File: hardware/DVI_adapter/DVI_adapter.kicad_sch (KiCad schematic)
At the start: 58 parts, among them J1 DF12NB(3.0)-30DS-0.5V(51), J2 DF12NB(3.0)-30DS-0.5V(51), J3 FPC Cable connector 1x20, U1 TXS0102DQE, U2 HE9009M6R, U2 TFP410

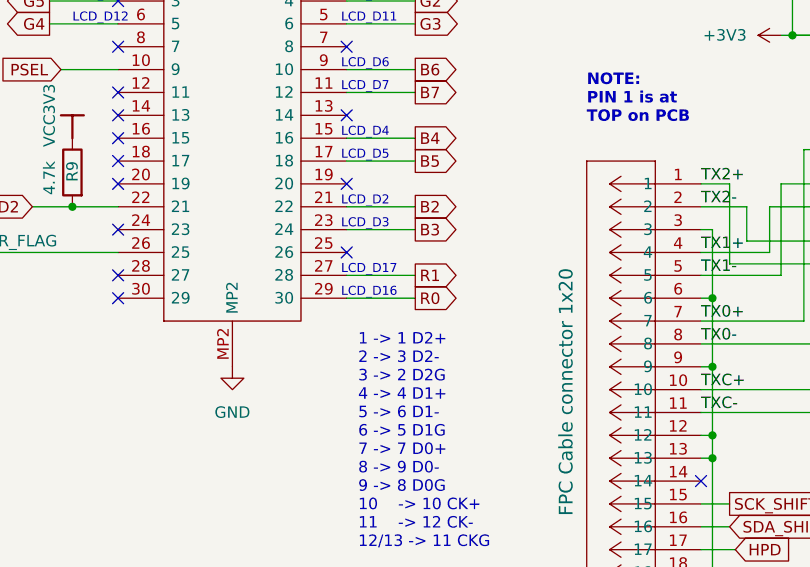
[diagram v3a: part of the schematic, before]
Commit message: fix R0/R1 mixup
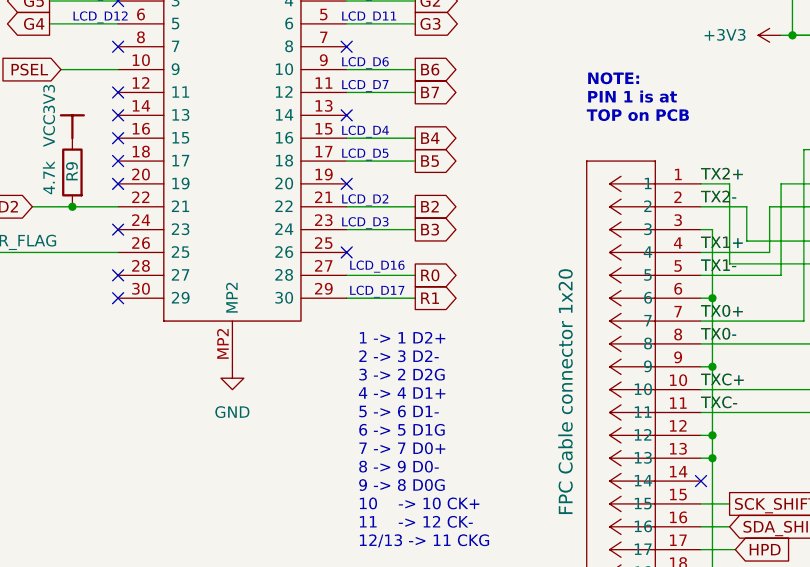
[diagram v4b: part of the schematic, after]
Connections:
- net R0: now also J2.27 (28); no longer J2.29 (30)
- net R1: now also J2.29 (30); no longer J2.27 (28)
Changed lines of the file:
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@@
+		)
+	)
+	(text "South connector"
+		(exclude_from_sim no)
+		(at 43.942 106.68 0)
+		(effects
+			(font
+				(size 1.27 1.27)
+			)
+			(justify right bottom)
+		)
+	)
+	(text "LCD_D15"
+		(exclude_from_sim no)
+		(at 61.595 78.74 0)
+		(effects
+			(font
+				(size 1 1)
+			)
+			(justify left bottom)
+		)
+	)
+	(text "LCD_D5"
+		(exclude_from_sim no)
+		(at 60.325 134.62 0)
+		(effects
+			(font
+				(size 1 1)
+			)
+			(justify left bottom)
+		)
+	)
+	(text "1 -> 1 D2+\n2 -> 3 D2-\n3 -> 2 D2G\n4 -> 4 D1+\n5 -> 6 D1-\n6 -> 5 D1G\n7 -> 7 D0+\n8 -> 9 D0-\n9 -> 8 D0G\n10    -> 10 CK+\n11    -> 12 CK-\n12/13 -> 11 CKG\n\n14 -> 13 CEC\n      14 NC\n15 -> 15 SCL\n16 -> 16 SDA\n      17 GND\n17 -> 19 HPD\n18/19/20 -> 18 +5V\nGND   20 SHIELD"
+		(exclude_from_sim no)
+		(at 62.23 175.006 0)
+		(effects
+			(font
+				(size 1.27 1.27)
+			)
+			(justify left)
+		)
+	)
+	(text "North connector"
+		(exclude_from_sim no)
+		(at 44.196 44.196 0)
+		(effects
+			(font
+				(size 1.27 1.27)
+			)
+			(justify right bottom)
+		)
+	)
+	(text "LCD_D1"
+		(exclude_from_sim no)
+		(at 31.75 50.8 0)
+		(effects
+			(font
+				(size 1 1)
+			)
+			(justify left bottom)
+		)
+	)
+	(text "LCD_D13"
+		(exclude_from_sim no)
+		(at 30.48 116.84 0)
+		(effects
+			(font
+				(size 1 1)
+			)
+			(justify left bottom)
+		)
+	)
+	(text "LCD_D9"
+		(exclude_from_sim no)
+		(at 31.75 66.04 0)
+		(effects
+			(font
+				(size 1 1)
+			)
+			(justify left bottom)
+		)
+	)
+	(text "LCD_D2"
+		(exclude_from_sim no)
+		(at 60.325 139.7 0)
+		(effects
+			(font
+				(size 1 1)
+			)
+			(justify left bottom)
+		)
+	)
+	(text "LCD_D18"
+		(exclude_from_sim no)
+		(at 61.595 68.58 0)
+		(effects
+			(font
+				(size 1 1)
+			)
+			(justify left bottom)
 		)
 	)
 	(text "LCD_D16"
 		(exclude_from_sim no)
-		(at 60.325 149.86 0)
-		(effects
-			(font
-				(size 1 1)
-			)
-			(justify left bottom)
-		)
-	)
-	(text "LCD_D17"
-		(exclude_from_sim no)
-		(at 60.325 147.32 0)
-		(effects
-			(font
-				(size 1 1)
-			)
-			(justify left bottom)
-		)
-	)
-	(text "South connector"
-		(exclude_from_sim no)
-		(at 43.942 106.68 0)
-		(effects
-			(font
-				(size 1.27 1.27)
-			)
-			(justify right bottom)
-		)
-	)
-	(text "LCD_D15"
-		(exclude_from_sim no)
-		(at 61.595 78.74 0)
-		(effects
-			(font
-				(size 1 1)
-			)
-			(justify left bottom)
-		)
-	)
-	(text "LCD_D5"
-		(exclude_from_sim no)
-		(at 60.325 134.62 0)
-		(effects
-			(font
-				(size 1 1)
-			)
-			(justify left bottom)
-		)
-	)
-	(text "1 -> 1 D2+\n2 -> 3 D2-\n3 -> 2 D2G\n4 -> 4 D1+\n5 -> 6 D1-\n6 -> 5 D1G\n7 -> 7 D0+\n8 -> 9 D0-\n9 -> 8 D0G\n10    -> 10 CK+\n11    -> 12 CK-\n12/13 -> 11 CKG\n\n14 -> 13 CEC\n      14 NC\n15 -> 15 SCL\n16 -> 16 SDA\n      17 GND\n17 -> 19 HPD\n18/19/20 -> 18 +5V\nGND   20 SHIELD"
-		(exclude_from_sim no)
-		(at 62.23 175.006 0)
-		(effects
-			(font
-				(size 1.27 1.27)
-			)
-			(justify left)
-		)
-	)
-	(text "North connector"
-		(exclude_from_sim no)
-		(at 44.196 44.196 0)
-		(effects
-			(font
-				(size 1.27 1.27)
-			)
-			(justify right bottom)
-		)
-	)
-	(text "LCD_D1"
-		(exclude_from_sim no)
-		(at 31.75 50.8 0)
-		(effects
-			(font
-				(size 1 1)
-			)
-			(justify left bottom)
-		)
-	)
-	(text "LCD_D13"
-		(exclude_from_sim no)
-		(at 30.48 116.84 0)
-		(effects
-			(font
-				(size 1 1)
-			)
-			(justify left bottom)
-		)
-	)
-	(text "LCD_D9"
-		(exclude_from_sim no)
-		(at 31.75 66.04 0)
-		(effects
-			(font
-				(size 1 1)
-			)
-			(justify left bottom)
-		)
-	)
-	(text "LCD_D2"
-		(exclude_from_sim no)
-		(at 60.325 139.7 0)
-		(effects
-			(font
-				(size 1 1)
-			)
-			(justify left bottom)
-		)
-	)
-	(text "LCD_D18"
-		(exclude_from_sim no)
-		(at 61.595 68.58 0)
+		(at 61.214 147.066 0)
 		(effects
 			(font
@@
 		)
 	)
+	(text "LCD_D17"
+		(exclude_from_sim no)
+		(at 61.214 149.86 0)
+		(effects
+			(font
+				(size 1 1)
+			)
+			(justify left bottom)
+		)
+	)
 	(text "NOTE:\nPIN 1 is at \nTOP on PCB"
 		(exclude_from_sim no)
@@
 		)
 	)
+	(global_label "R0"
+		(shape output)
+		(at 68.58 147.32 0)
+		(fields_autoplaced yes)
+		(effects
+			(font
+				(size 1.27 1.27)
+			)
+			(justify left)
+		)
+		(property "Intersheetrefs" "${INTERSHEET_REFS}"
+			(at 74.0447 147.32 0)
+			(effects
+				(font
+					(size 1.27 1.27)
+				)
+				(justify left)
+				(hide yes)
+			)
+		)
+	)
 	(global_label "G3"
 		(shape output)
@@
 		)
 	)
-	(global_label "R0"
-		(shape output)
-		(at 68.58 149.86 0)
-		(fields_autoplaced yes)
-		(effects
-			(font
-				(size 1.27 1.27)
-			)
-			(justify left)
-		)
-		(property "Intersheetrefs" "${INTERSHEET_REFS}"
-			(at 74.0447 149.86 0)
-			(effects
-				(font
-					(size 1.27 1.27)
-				)
-				(justify left)
-				(hide yes)
-			)
-		)
-	)
 	(global_label "LCD_DE"
 		(shape input)
@@
 		)
 	)
+	(global_label "R1"
+		(shape output)
+		(at 68.58 149.86 0)
+		(fields_autoplaced yes)
+		(effects
+			(font
+				(size 1.27 1.27)
+			)
+			(justify left)
+		)
+		(property "Intersheetrefs" "${INTERSHEET_REFS}"
+			(at 74.0447 149.86 0)
+			(effects
+				(font
+					(size 1.27 1.27)
+				)
+				(justify left)
+				(hide yes)
+			)
+		)
+	)
 	(global_label "SDA"
 		(shape bidirectional)
@@
 				(hide yes)
 			)
-		)
-	)
-	(global_label "R1"
-		(shape output)
-		(at 68.58 147.32 0)
-		(fields_autoplaced yes)
-		(effects
-			(font
-				(size 1.27 1.27)
-			)
-			(justify left)
-		)
-		(property "Intersheetrefs" "${INTERSHEET_REFS}"
-			(at 74.0447 147.32 0)
-			(effects
-				(font
-					(size 1.27 1.27)
-				)
-				(justify left)
-				(hide yes)
-			)

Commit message: fixes for producion and notes
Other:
- note added: "FIXES: Add test points Add auto reset Add HPD connection to HTPLG (pin 9) - use solder jumper and 1k series resistor CTL1/2/3 has pulldowns so jumpers should connect to DVDD PRG18BB330MB1RB drops 2V with a powered HDMI to VGA adapter (77mA consumption) ***D1/D2 does not seems properly soldered*** NEW NOTES: -pin 1 of FPC conector is bad in silkscreen NOTE: LCD_DE & PCLK were inverted in a previou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"
- note removed: "FIXES: Add test points Add auto reset Add HPD connection to HTPLG (pin 9) - use solder jumper and 1k series resistor CTL1/2/3 has pulldowns so jumpers should connect to DVDD PRG18BB330MB1RB drops 2V with a powered HDMI to VGA adapter (77mA consumption) ***D1/D2 does not seems properly soldered*** NOTE: LCD_DE & PCLK were inverted in a previous version"
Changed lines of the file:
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@@
 		)
 	)
-	(text "FIXES:\nAdd test points\nAdd auto reset\nAdd HPD connection to HTPLG (pin 9) - use solder jumper and 1k series resistor\nCTL1/2/3 has pulldowns so jumpers should connect to DVDD\nPRG18BB330MB1RB drops 2V with a powered HDMI to VGA adapter (77mA consumption)\n\n***D1/D2 does not seems properly soldered***\n\n\n\nNOTE:\nLCD_DE & PCLK were inverted in a previous version\n"
+	(text "FIXES:\nAdd test points\nAdd auto reset\nAdd HPD connection to HTPLG (pin 9) - use solder jumper and 1k series resistor\nCTL1/2/3 has pulldowns so jumpers should connect to DVDD\nPRG18BB330MB1RB drops 2V with a powered HDMI to VGA adapter (77mA consumption)\n\n***D1/D2 does not seems properly soldered***\n\nNEW NOTES:\n-pin 1 of FPC conector is bad in silkscreen\n\n\n\nNOTE:\nLCD_DE & PCLK were inverted in a previous version\n"
 		(exclude_from_sim no)
 		(at 19.304 13.97 0)
